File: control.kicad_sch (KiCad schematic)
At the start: 1 part, among them U16001 Opamp_Dual

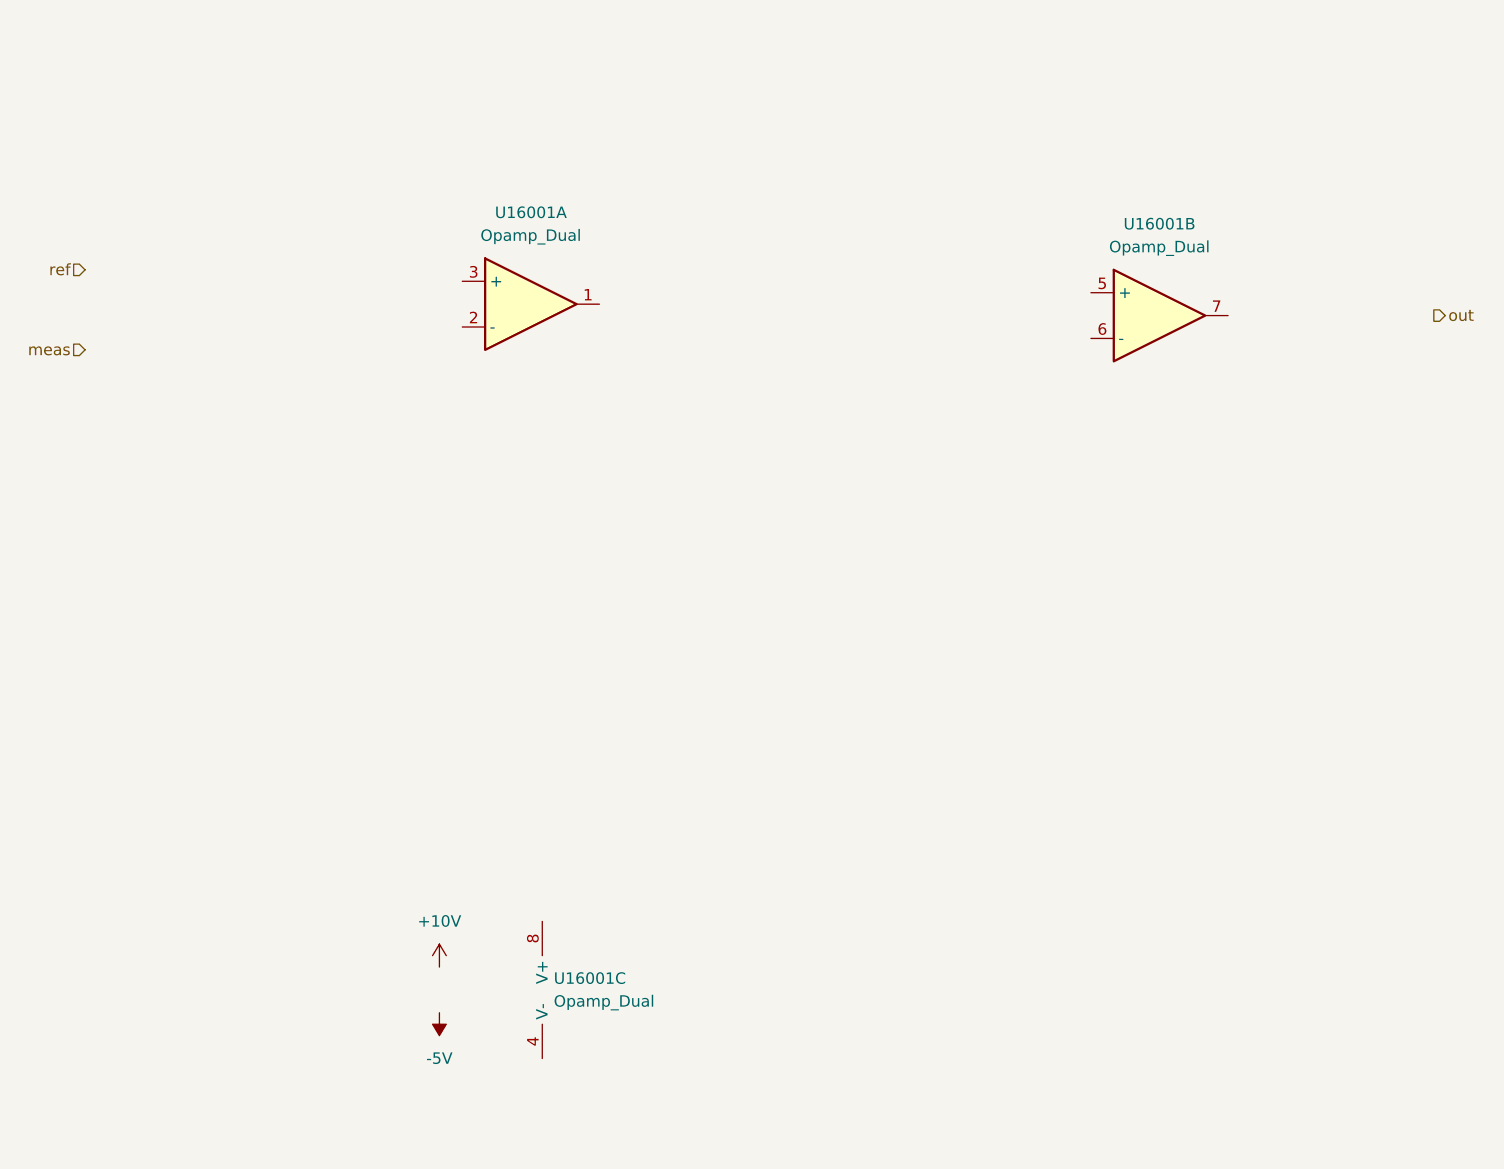
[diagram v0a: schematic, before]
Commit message: add control subtraction junction
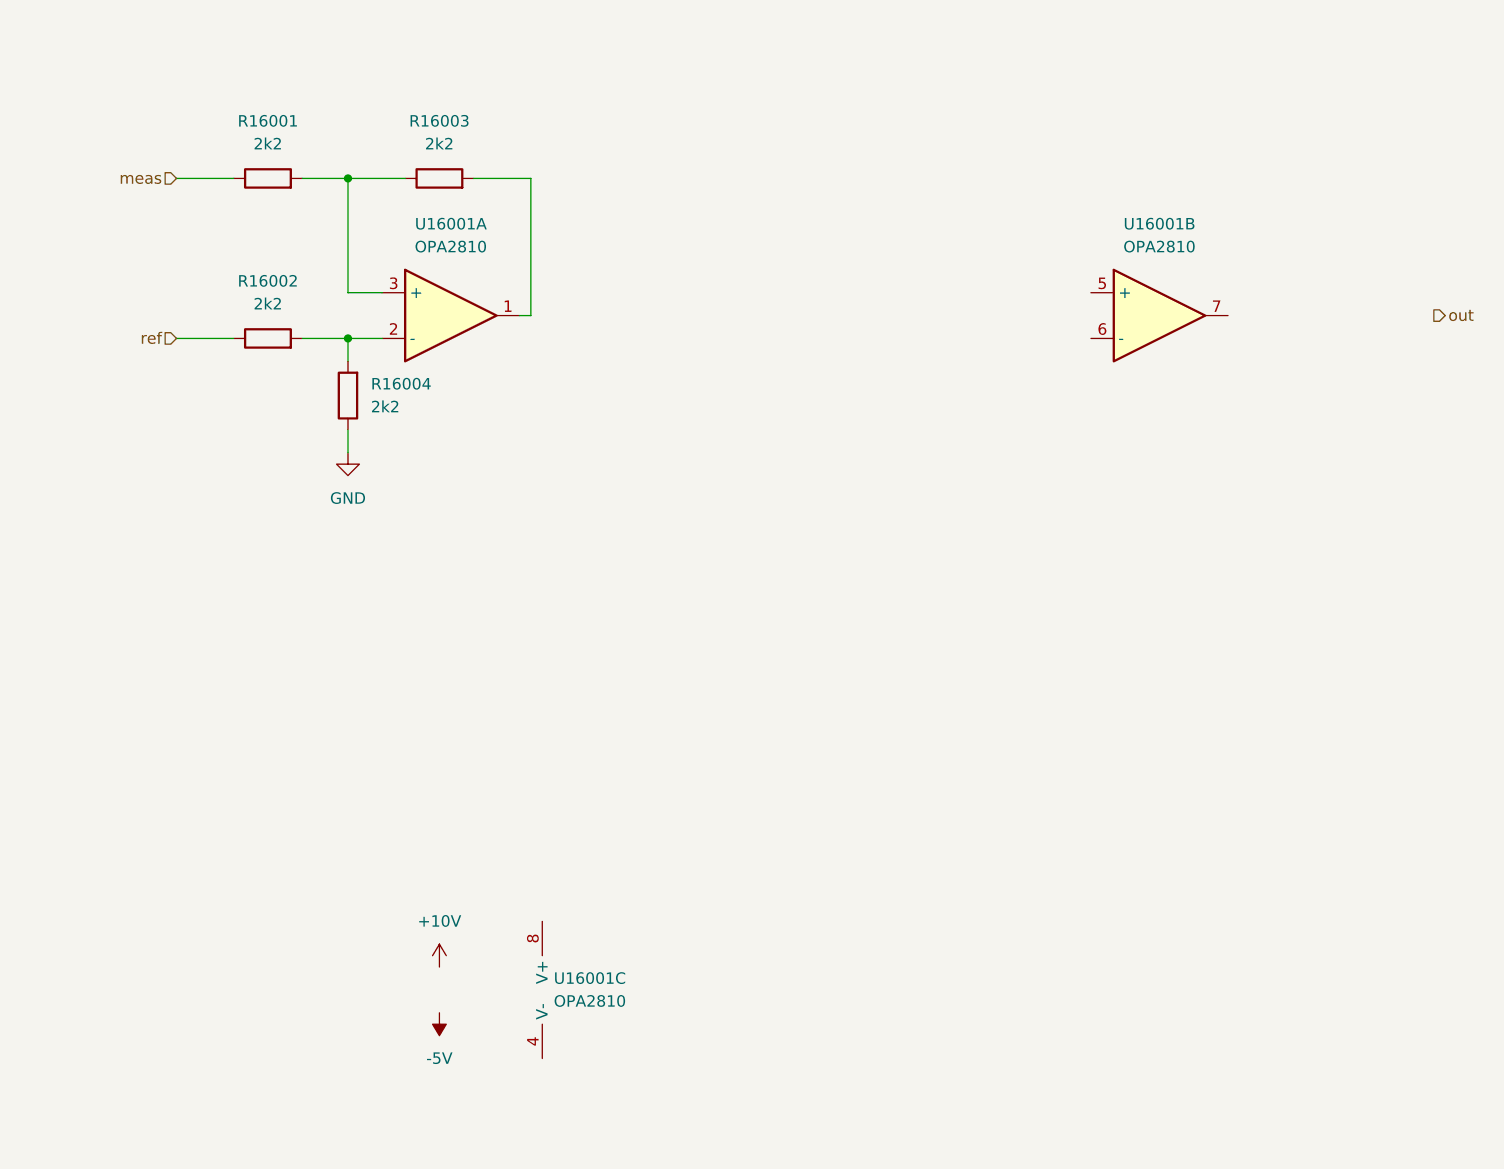
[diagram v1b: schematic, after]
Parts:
- added R16001, R16002, R16003, R16004: 2k2, Resistor_SMD:R_1210_3225Metric_Pad1.30x2.65mm_HandSolder, symbol Device:R
- U16001: value Opamp_Dual -> OPA2810
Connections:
- net meas: now also R16001.1
- net ref: now also R16002.1
- net at U16001.1: now also R16003.2
- net at U16001.2 (-): now also R16002.2, R16004.2
- net at U16001.3 (+): now also R16001.2, R16003.1
- new net GND: R16004.1
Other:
- moved on the sheet: U16001A

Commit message: add control pid circuit
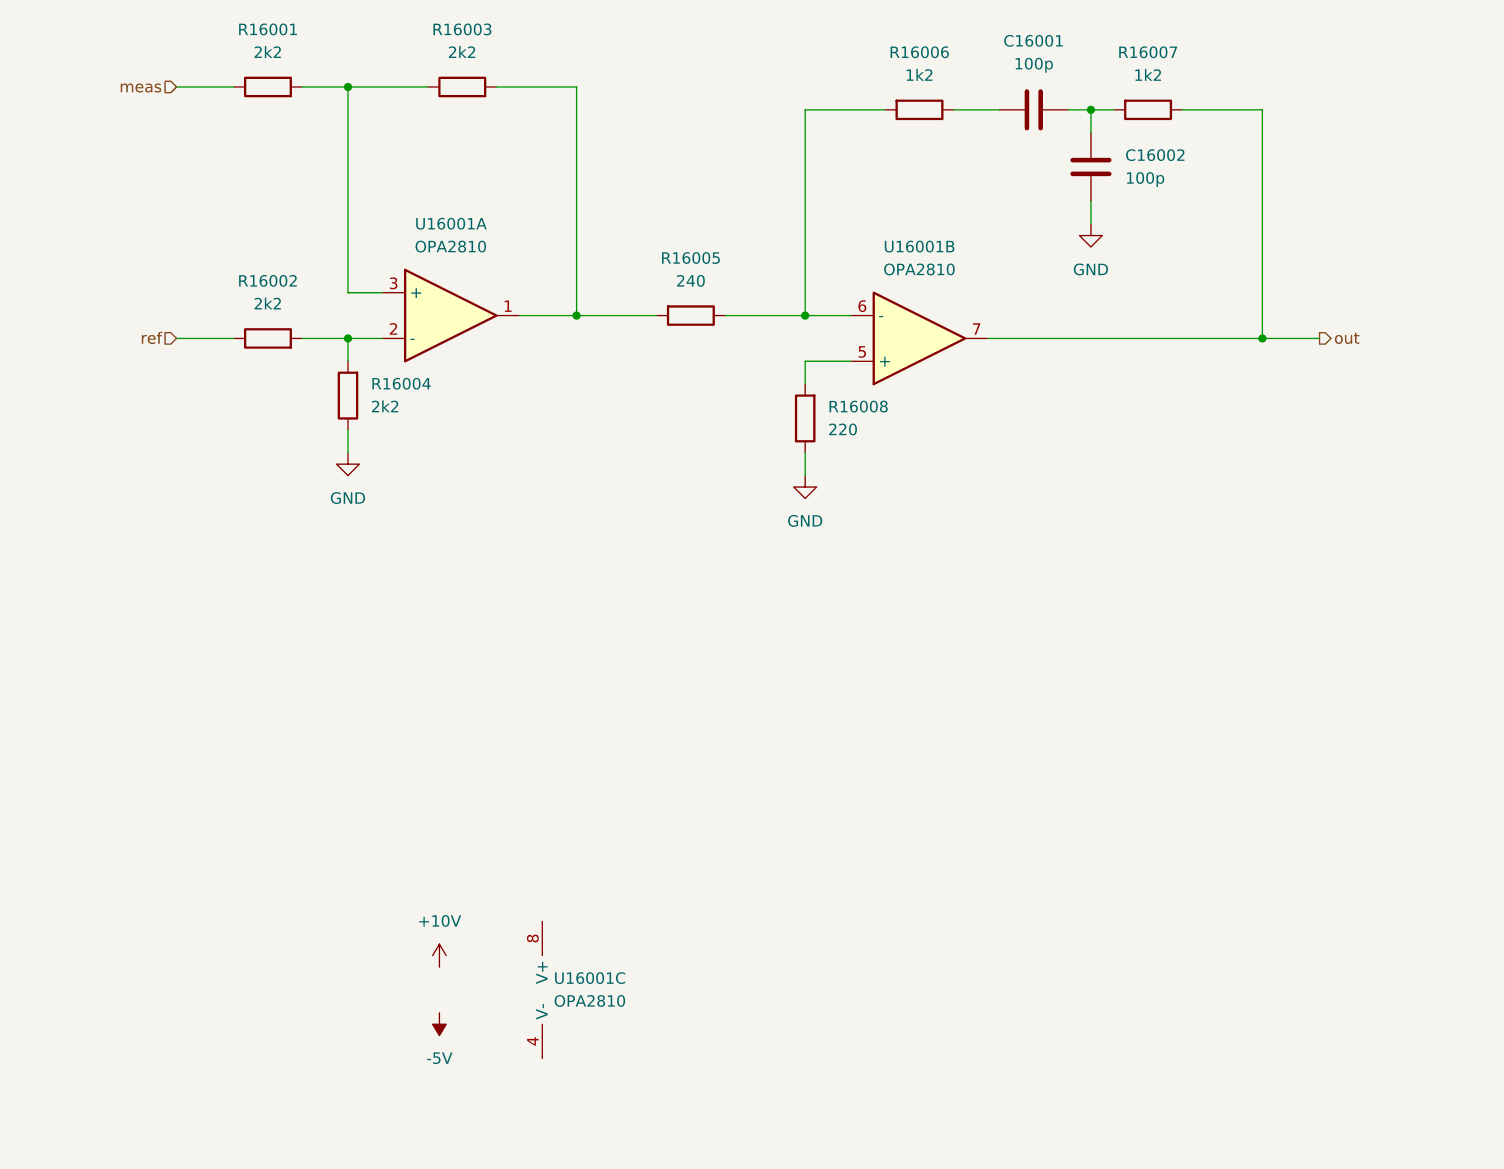
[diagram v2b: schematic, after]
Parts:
- added C16001, C16002: 100p, Capacitor_SMD:C_0805_2012Metric_Pad1.18x1.45mm_HandSolder, symbol Device:C
- added R16005: 240, Resistor_SMD:R_1210_3225Metric_Pad1.30x2.65mm_HandSolder, symbol Device:R
- added R16006, R16007: 1k2, Resistor_SMD:R_1210_3225Metric_Pad1.30x2.65mm_HandSolder, symbol Device:R
- added R16008: 220, Resistor_SMD:R_1210_3225Metric_Pad1.30x2.65mm_HandSolder, symbol Device:R
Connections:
- net GND: now also C16002.2, R16008.1
- net out: now also U16001.7, R16007.1
- net at R16003.2, U16001.1: now also R16005.2
- net at U16001.5 (+): now also R16008.2
- net at U16001.6 (-): now also R16005.1, R16006.2
- new net: C16001.1, R16006.1
- new net: C16001.2, C16002.1, R16007.2
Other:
- moved on the sheet: R16001, R16003, U16001B

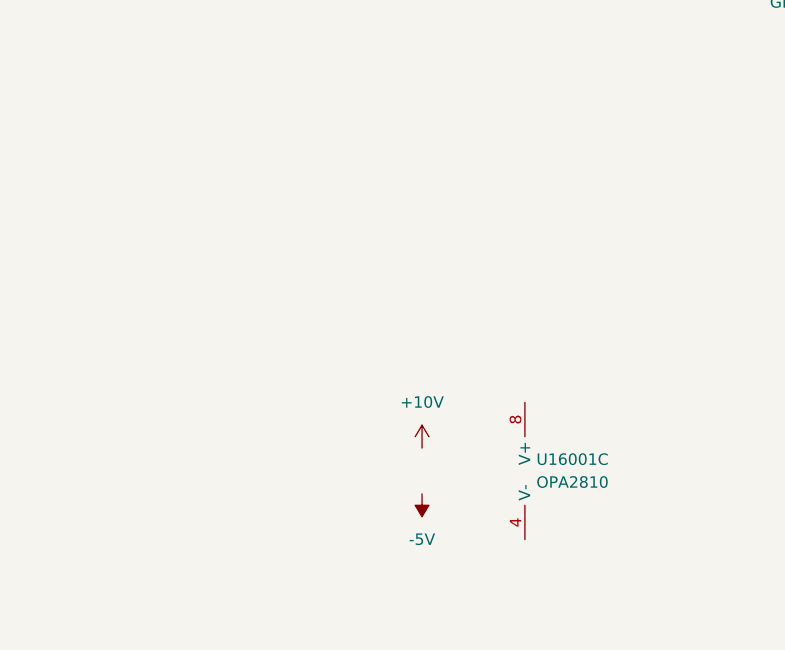
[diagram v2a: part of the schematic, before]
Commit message: add control opamp power decoupling
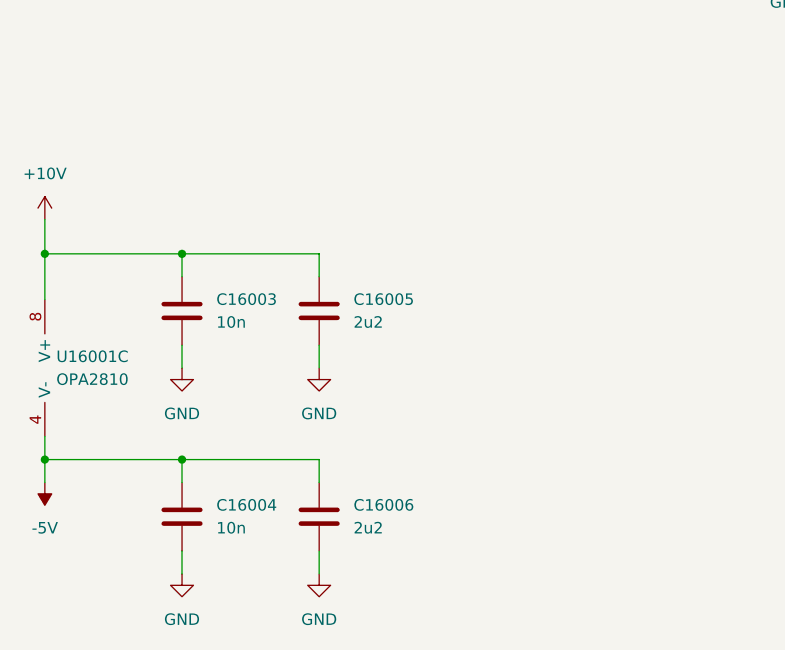
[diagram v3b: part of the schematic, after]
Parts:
- added C16003, C16004: 10n, Capacitor_SMD:C_0805_2012Metric_Pad1.18x1.45mm_HandSolder, symbol Device:C
- added C16005, C16006: 2u2, Capacitor_SMD:C_0805_2012Metric_Pad1.18x1.45mm_HandSolder, symbol Device:C
- R16008: MPN RC1210FR-07220RL -> RC1210FR-07220RL
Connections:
- net +10V: now also U16001.8 (V+), C16003.1, C16005.1
- net -5V: now also U16001.4 (V-), C16004.1, C16006.1
- net GND: now also C16003.2, C16004.2, C16005.2, C16006.2
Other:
- moved on the sheet: U16001C
